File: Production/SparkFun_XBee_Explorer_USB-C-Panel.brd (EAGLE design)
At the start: 35.6 x 59.7 mm, 109 parts, among them J3 USB Female Type C Connector, J4 QWIIC_RIGHT_ANGLE, U2 AP63203, U5 ESD Diode, U7 FT231XS

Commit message: Adds Production Files
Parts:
- removed FRAME1: FRAME-LEDGER, SparkFun-Aesthetics:CREATIVE_COMMONS
- added ALED1, ALED2, ALED3, PLED1, PLED2, PLED3, RLED1, RLED2, RLED3, SHLD1, SHLD2, SHLD3: JUMPER-SMT_2_NC_TRACE_SILK, SparkFun-Jumpers:SMT-JUMPER_2_NC_TRACE_SILK
- added C13, C20, C22, C23, C27, C33, C35, C36, C40, C46, C48, C49: 0.1uF, SparkFun-Capacitors:0603
- added C15, C16, C28, C29, C41, C42: 22uF, SparkFun-Capacitors:0603
- added C17, C30, C43: 10uF, SparkFun-Capacitors:1210
- added C18, C19, C31, C32, C44, C45: 10nF, SparkFun-Capacitors:0603
- added C21, C34, C47: 10uF, SparkFun-Capacitors:0603
- added C24, C37, C50: 47pF, SparkFun-Capacitors:0603
- added C25, C38, C51: 10pF, SparkFun-Capacitors:0603
- added C26, C39, C52: 4.7uF, SparkFun-Capacitors:0603
- added D1, D10, D7: Red, SparkFun-LED:LED-0603
- added D11, D5, D8: BLUE, SparkFun-LED:LED-0603
- added D12, D6, D9: Yellow, SparkFun-LED:LED-0603
- added E$1, E$2, E$3, E$4: (no value), SparkFun-Aesthetics:FIDUCIAL-1X2
- added E$5, E$6: (no value), SparkFun-Retired:FIDUCIAL-1.5X3
- added FD10, FD11, FD12, FD13, FD14, FD15, FD16, FD5, FD6, FD7, FD8, FD9: FIDUCIAL1X2, SparkFun-Aesthetics:FIDUCIAL-1X2
- added H10, H11, H12, H13, H14, H15, H16, H5, H6, H7, H8, H9: STAND-OFFTIGHT, SparkFun-Hardware:STAND-OFF-TIGHT
- added I2C_PU1, I2C_PU2, I2C_PU3: JUMPER-SMT_3_2-NC_TRACE_SILK, SparkFun-Jumpers:SMT-JUMPER_3_2-NC_TRACE_SILK
- added J10, J16, J17, J23, J24, J9: (no value), SparkFun-Connectors:1X10_NO_SILK
- added J11, J18, J25: (no value), xbee_smart_modem:XBEE3-SMD
- added J12, J19, J26: USB Female Type C Connector, SparkFun-Connectors:USB-C-16P-4LAYER-ISOLATED
- added J13, J14, J20, J21, J27, J28: (no value), SparkFun-Connectors:1X01_NO_SILK_STAND
- added J15, J22, J7: QWIIC_RIGHT_ANGLE, SparkFun-Connectors:JST04_1MM_RA
- added L2, L3, L4: 3.9UH, SparkFun-Coils:INDUCTOR_3.9UH
- added LOGO10, LOGO7: OSHW-LOGOS, SparkFun-Aesthetics:OSHW-LOGO-S
- added LOGO11, LOGO5, LOGO8: QWIIC_LOGO_4MM, SparkFun-Aesthetics:QWIIC_4MM
- added LOGO12, LOGO6, LOGO9: SFE_LOGO_NAME.2_INCH, SparkFun-Aesthetics:SFE_LOGO_NAME_.2
- added R1, R10, R17, R18, R20, R22, R25, R26, R28, R30, R4, R6: 2.2k, SparkFun-Resistors:0603
- added R13, R16, R23, R24, R31, R32: 5.1k, SparkFun-Resistors:0603
- added R19, R27, R5: 4.7k, SparkFun-Resistors:0603
- added R21, R29, R9: 10k, SparkFun-Resistors:0603
- added S3, S4, S5, S6, S7, S8: (no value), SparkFun-Switches:TACTILE_SWITCH_SMD_5.2MM
- added U$100, U$125, U$154, U$179, U$208, U$71: (no value), topmirror:#GND#0
- added U$101, U$102, U$155, U$156, U$209, U$210: (no value), top:XBEE340
- added U$103, U$157, U$211: (no value), top:ASC32
- added U$104, U$158, U$212: (no value), top:RSSI31
- added U$105, U$159, U$213: (no value), top:PWR29
- added U$106, U$160, U$214: (no value), topmirror:#D1#AD1#SCL#8
- added U$107, U$108, U$161, U$162, U$215, U$216: (no value), top:EXPLORER1344
- added U$109, U$111, U$163, U$165, U$33, U$39: (no value), top:#3V3#1
- added U$110, U$164, U$34: (no value), top:#I2C#33
- added U$112, U$146, U$166, U$200, U$41, U$92: (no value), top:#VIN#4
- added U$113, U$167, U$42: (no value), bot:D03
- added U$114, U$168, U$43: (no value), top:#RST#30
- added U$115, U$169, U$47: (no value), SparkFun-Aesthetics:SFE_LOGO_NAME_.2
- added U$116, U$170, U$50: (no value), SparkFun-Aesthetics:SFE_LOGO_FLAME_.2
- added U$117, U$171, U$53: (no value), topmirror:#D0#AD0#18
- added U$118, U$172, U$55: (no value), topmirror:#D2#AD2#19
- added U$119, U$173, U$56: (no value), topmirror:#D3#AD3#23
- added U$120, U$174, U$57: (no value), topmirror:#D6##RTS##25
- added U$121, U$175, U$62: (no value), topmirror:#D5#ASSOC#25
- added U$122, U$176, U$68: (no value), topmirror:#D9##SLP##28
- added U$123, U$177, U$69: (no value), topmirror:#D7##CTS##26
- added U$124, U$178, U$70: (no value), topmirror:#D4#PICO#25
- added U$126, U$180, U$72: (no value), topmirror:#D8##DTR##27
- added U$127, U$181, U$73: (no value), topmirror:#RSSI#D10#17
- added U$128, U$182, U$74: (no value), topmirror:#SDA#D11#9
- added U$129, U$183, U$75: (no value), topmirror:##RST##15
- added U$130, U$184, U$76: (no value), topmirror:#POCI#D12#24
- added U$131, U$185, U$77: (no value), topmirror:#RXI#D14#15
- added U$132, U$186, U$78: (no value), topmirror:#TXO#D13#13
- added U$133, U$187, U$79: (no value), topmirror:#EN#17
- added U$134, U$188, U$80: (no value), topmirror:#ALED#21
- added U$135, U$189, U$81: (no value), topmirror:#RLED#22
- added U$136, U$190, U$82: (no value), topmirror:#PLED#20
- added U$137, U$191, U$83: (no value), botmirror:#TXO#8
- added U$138, U$192, U$84: (no value), botmirror:#RXI#7
- added U$139, U$193, U$85: (no value), botmirror:#POCI#32
- added U$140, U$194, U$86: (no value), botmirror:##RST##13
- added U$141, U$195, U$87: (no value), botmirror:##RTS##14
- added U$142, U$196, U$88: (no value), botmirror:##CS##26
- added U$143, U$197, U$89: (no value), botmirror:#SCLK#33
- added U$144, U$198, U$90: (no value), botmirror:#SCL#9
- added U$145, U$199, U$91: (no value), botmirror:#D0#3
- added U$147, U$201, U$93: (no value), botmirror:#EN#15
- added U$148, U$202, U$94: (no value), topmirror:#SHLD#36
- added U$149, U$203, U$95: (no value), topmirror:#NC#1
- added U$150, U$204, U$96: (no value), botmirror:#NC#3
- added U$151, U$152, U$205, U$206, U$97, U$98: (no value), topmirror:USB#C1342
- added U$153, U$207, U$99: (no value), topmirror:UART34
- added U1, U10, U6: AP63203, SparkFun-IC-Power:SOT23-6
- added U11, U3, U8: ESD Diode, SparkFun-DiscreteSemi:SOT-23-6
- added U12, U4, U9: FT231XS, SparkFun-IC-Comms:SSOP20_L
- LOGO4: value SPECIAL_INSTRUCTIONS-ORDERING -> OSHW-LOGOS; device SparkFun-Aesthetics:ORDERING_INSTRUCTIONS -> SparkFun-Aesthetics:OSHW-LOGO-S
- moved LOGO4 25.8 mm to (69.3, 53.0)
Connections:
- new net !RESET!1: C18.1, J10.5, J11.5, S3.1, S3.2
- new net !RESET!2: C31.1, J17.5, J18.5, S5.1, S5.2
- new net !RESET!3: C44.1, J24.5, J25.5, S7.1, S7.2
- new net 3.3V1: C15.1, C16.1, C19.1, C20.1, C21.1, C22.1, C23.1, C24.1, C25.1, C26.1, I2C_PU1.2, J10.1, J11.1, J7.2, L2.P$2, R5.1, U1.1, U4.13, U4.14, U4.15, U4.3
- new net 3.3V2: C28.1, C29.1, C32.1, C33.1, C34.1, C35.1, C36.1, C37.1, C38.1, C39.1, I2C_PU2.2, J15.2, J17.1, J18.1, L3.P$2, R19.1, U6.1, U9.13, U9.14, U9.15, U9.3
- new net 3.3V3: C41.1, C42.1, C45.1, C46.1, C47.1, C48.1, C49.1, C50.1, C51.1, C52.1, I2C_PU3.2, J22.2, J24.1, J25.1, L4.P$2, R27.1, U10.1, U12.13, U12.14, U12.15, U12.3
- new net D+1: J12.A6, J12.B6, U3.6, U4.11
- new net D+2: J19.A6, J19.B6, U8.6, U9.11
- new net D+3: J26.A6, J26.B6, U11.6, U12.11
- new net D-1: J12.A7, J12.B7, U3.4, U4.12
- new net D-2: J19.A7, J19.B7, U8.4, U9.12
- new net D-3: J26.A7, J26.B7, U11.4, U12.12
- new net D1: J11.20, J9.1, S4.1, S4.2
- new net D1/SCL1: J11.19, J7.4, J9.2, R4.1
- new net D1/SCL2: J15.4, J16.2, J18.19, R18.1
- new net D1/SCL3: J22.4, J23.2, J25.19, R26.1
- new net D10/RSSI_PWM1: J10.6, J11.6, R10.1
- new net D10/RSSI_PWM2: J17.6, J18.6, R22.1
- new net D10/RSSI_PWM3: J24.6, J25.6, R30.1
- new net D11/SDA1: J10.7, J11.7, J7.3, R1.1
- new net D11/SDA2: J15.3, J17.7, J18.7, R17.1
- new net D11/SDA3: J22.3, J24.7, J25.7, R25.1
- new net D12/SPI_POCI1: J10.4, J11.4
- new net D12/SPI_POCI2: J17.4, J18.4
- new net D12/SPI_POCI3: J24.4, J25.4
- new net D13/TXO1: J10.2, J11.2, U4.4
- new net D13/TXO2: J17.2, J18.2, U9.4
- new net D13/TXO3: J24.2, J25.2, U12.4
- new net D14/RXI1: J10.3, J11.3, U4.20
- new net D14/RXI2: J17.3, J18.3, U9.20
- new net D14/RXI3: J24.3, J25.3, U12.20
- new net D2: J16.1, J18.20, S6.1, S6.2
- new net D2/SPI_CLK1: J11.18, J9.3
- new net D2/SPI_CLK2: J16.3, J18.18
- new net D2/SPI_CLK3: J23.3, J25.18
- new net D3: J23.1, J25.20, S8.1, S8.2
- new net D3/SPI_!CS!1: J11.17, J9.4
- new net D3/SPI_!CS!2: J16.4, J18.17
- new net D3/SPI_!CS!3: J23.4, J25.17
- new net D4/SPI_PICO1: J11.11, J9.10
- new net D4/SPI_PICO2: J16.10, J18.11
- new net D4/SPI_PICO3: J23.10, J25.11
- new net D5/ASSOCIATE1: J11.15, J9.6, R6.1
- new net D5/ASSOCIATE2: J16.6, J18.15, R20.1
- new net D5/ASSOCIATE3: J23.6, J25.15, R28.1
- new net D6/!RTS!1: J11.16, J9.5, U4.2
- new net D6/!RTS!2: J16.5, J18.16, U9.2
- new net D6/!RTS!3: J23.5, J25.16, U12.2
- new net D7/!CTS!1: J11.12, J9.9, U4.9
- new net D7/!CTS!2: J16.9, J18.12, U9.9
- new net D7/!CTS!3: J23.9, J25.12, U12.9
- new net D8/!DTR!1: J10.9, J11.9, U4.1
- new net D8/!DTR!2: J17.9, J18.9, U9.1
- new net D8/!DTR!3: J24.9, J25.9, U12.1
- new net D9/!SLEEP!1: J11.13, J9.8
- new net D9/!SLEEP!2: J16.8, J18.13
- new net D9/!SLEEP!3: J23.8, J25.13
- new net EN1: J14.1, R9.1, U1.2
- new net EN2: J21.1, R21.1, U6.2
- new net EN3: J28.1, R29.1, U10.2
- new net GND1: ALED1.1, C15.2, C16.2, C17.2, C18.2, C19.2, C20.2, C21.2, C22.2, C23.2, C24.2, C25.2, C26.2, J10.10, J11.10, J12.GND, J12.GND2, J7.1, PLED1.1, R13.1, R16.1, RLED1.1, S3.3, S3.4, S4.3, S4.4, SHLD1.1, U1.4, U3.2, U4.16, U4.6
- new net GND2: ALED2.1, C28.2, C29.2, C30.2, C31.2, C32.2, C33.2, C34.2, C35.2, C36.2, C37.2, C38.2, C39.2, J15.1, J17.10, J18.10, J19.GND, J19.GND2, PLED2.1, R23.1, R24.1, RLED2.1, S5.3, S5.4, S6.3, S6.4, SHLD2.1, U6.4, U8.2, U9.16, U9.6
- new net GND3: ALED3.1, C41.2, C42.2, C43.2, C44.2, C45.2, C46.2, C47.2, C48.2, C49.2, C50.2, C51.2, C52.2, J22.1, J24.10, J25.10, J26.GND, J26.GND2, PLED3.1, R31.1, R32.1, RLED3.1, S7.3, S7.4, S8.3, S8.4, SHLD3.1, U10.4, U11.2, U12.16, U12.6
- new net N$10: D1.A, R5.2
- new net N$14: D5.A, R6.2
- new net N$15: ALED1.2, D5.C
- new net N$16: D1.C, PLED1.2
- new net N$17: C13.1, U1.6
- new net N$18: C13.2, L2.P$1, U1.5
- new net N$19: D6.A, R10.2
- new net N$20: D6.C, RLED1.2
- new net N$22: J12.B5, R16.2
- new net N$24: J12.A5, R13.2
- new net N$25: I2C_PU2.3, R17.2
- new net N$26: I2C_PU2.1, R18.2
- new net N$27: D7.A, R19.2
- new net N$28: D8.A, R20.2
- new net N$29: ALED2.2, D8.C
- new net N$30: D7.C, PLED2.2
- new net N$31: C27.1, U6.6
- new net N$32: C27.2, L3.P$1, U6.5
- new net N$33: D9.A, R22.2
- new net N$34: D9.C, RLED2.2
- new net N$35: J19.B5, R24.2
- new net N$36: J19.A5, R23.2
- new net N$37: I2C_PU3.3, R25.2
- new net N$38: I2C_PU3.1, R26.2
- new net N$39: D10.A, R27.2
- new net N$4: I2C_PU1.3, R1.2
- new net N$40: D11.A, R28.2
- new net N$41: ALED3.2, D11.C
- new net N$42: D10.C, PLED3.2
- new net N$43: C40.1, U10.6
- new net N$44: C40.2, L4.P$1, U10.5
- new net N$45: D12.A, R30.2
- new net N$46: D12.C, RLED3.2
- new net N$47: J26.B5, R32.2
- new net N$48: J26.A5, R31.2
- new net N$9: I2C_PU1.1, R4.2
- new net SHLD1: J12.SHLD1, J12.SHLD2, J12.SHLD3, J12.SHLD4, J12.SHLD5, J12.SHLD6, J12.SHLD7, J12.SHLD8, SHLD1.2
- new net SHLD2: J19.SHLD1, J19.SHLD2, J19.SHLD3, J19.SHLD4, J19.SHLD5, J19.SHLD6, J19.SHLD7, J19.SHLD8, SHLD2.2
- new net SHLD3: J26.SHLD1, J26.SHLD2, J26.SHLD3, J26.SHLD4, J26.SHLD5, J26.SHLD6, J26.SHLD7, J26.SHLD8, SHLD3.2
- new net VIN1: C17.1, J12.VBUS1, J12.VBUS2, J13.1, R9.2, U1.3, U3.5
- new net VIN2: C30.1, J19.VBUS1, J19.VBUS2, J20.1, R21.2, U6.3, U8.5
- new net VIN3: C43.1, J26.VBUS1, J26.VBUS2, J27.1, R29.2, U10.3, U11.5
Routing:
- net D14/RXI3: track 0.00 -> 47.7 mm, vias 0 -> 2
- net D14/RXI2: track 0.00 -> 47.7 mm, vias 0 -> 2
- net D14/RXI1: track 0.00 -> 47.7 mm, vias 0 -> 2
- net D1/SCL3: track 0.00 -> 45.4 mm
- net D1/SCL1: track 0.00 -> 45.4 mm
- net D1/SCL2: track 0.00 -> 45.4 mm
- net D11/SDA2: track 0.00 -> 45.1 mm, vias 0 -> 1
- net D11/SDA1: track 0.00 -> 45.1 mm, vias 0 -> 1
- net D11/SDA3: track 0.00 -> 45.1 mm, vias 0 -> 1
- net D10/RSSI_PWM2: track 0.00 -> 44.8 mm, vias 0 -> 3
- net D10/RSSI_PWM3: track 0.00 -> 44.8 mm, vias 0 -> 3
- net D10/RSSI_PWM1: track 0.00 -> 44.8 mm, vias 0 -> 3
- net D13/TXO3: track 0.00 -> 42.6 mm, vias 0 -> 2
- net D13/TXO2: track 0.00 -> 42.6 mm, vias 0 -> 2
- net D13/TXO1: track 0.00 -> 42.6 mm, vias 0 -> 2
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- added copper zone on layer 1, net 3.3V1
- added copper zone on layer 15, net 3.3V1
- added copper zone on layer 1, net 3.3V2
- added copper zone on layer 15, net 3.3V2
- added copper zone on layer 1, net 3.3V3
- added copper zone on layer 15, net 3.3V3
- added copper zone on layer 1, net GND1
- added copper zone on layer 16, net GND1
- added copper zone on layer 2, net GND1
- added copper zone on layer 1, net GND2
- added copper zone on layer 16, net GND2
- added copper zone on layer 2, net GND2
- added copper zone on layer 1, net GND3
- added copper zone on layer 16, net GND3
- added copper zone on layer 2, net GND3
- added copper zone on layer 1, net N$18
- added copper zone on layer 1, net N$32
- added copper zone on layer 1, net N$44
- added copper zone on layer 1, net SHLD1
- added copper zone on layer 15, net SHLD1
- added copper zone on layer 16, net SHLD1
- added copper zone on layer 2, net SHLD1
- added copper zone on layer 1, net SHLD2
- added copper zone on layer 15, net SHLD2
- added copper zone on layer 16, net SHLD2
- added copper zone on layer 2, net SHLD2
- added copper zone on layer 1, net SHLD3
- added copper zone on layer 15, net SHLD3
- added copper zone on layer 16, net SHLD3
- added copper zone on layer 2, net SHLD3
- added copper zone on layer 1, net VIN1
- added copper zone on layer 1, net VIN2
- added copper zone on layer 1, net VIN3
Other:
- board size 35.6 x 59.7 mm -> 157.5 x 87.9 mm
- board text added: "Route Out"
- board text added: "v-score"
- board text removed: "1.6mm Thickness"
- board text removed: "Elias Santistevan"
- board text removed: "Four Layer Board"
- board text removed: "Lead Free HASL"
- board text removed: "Units in Inches"

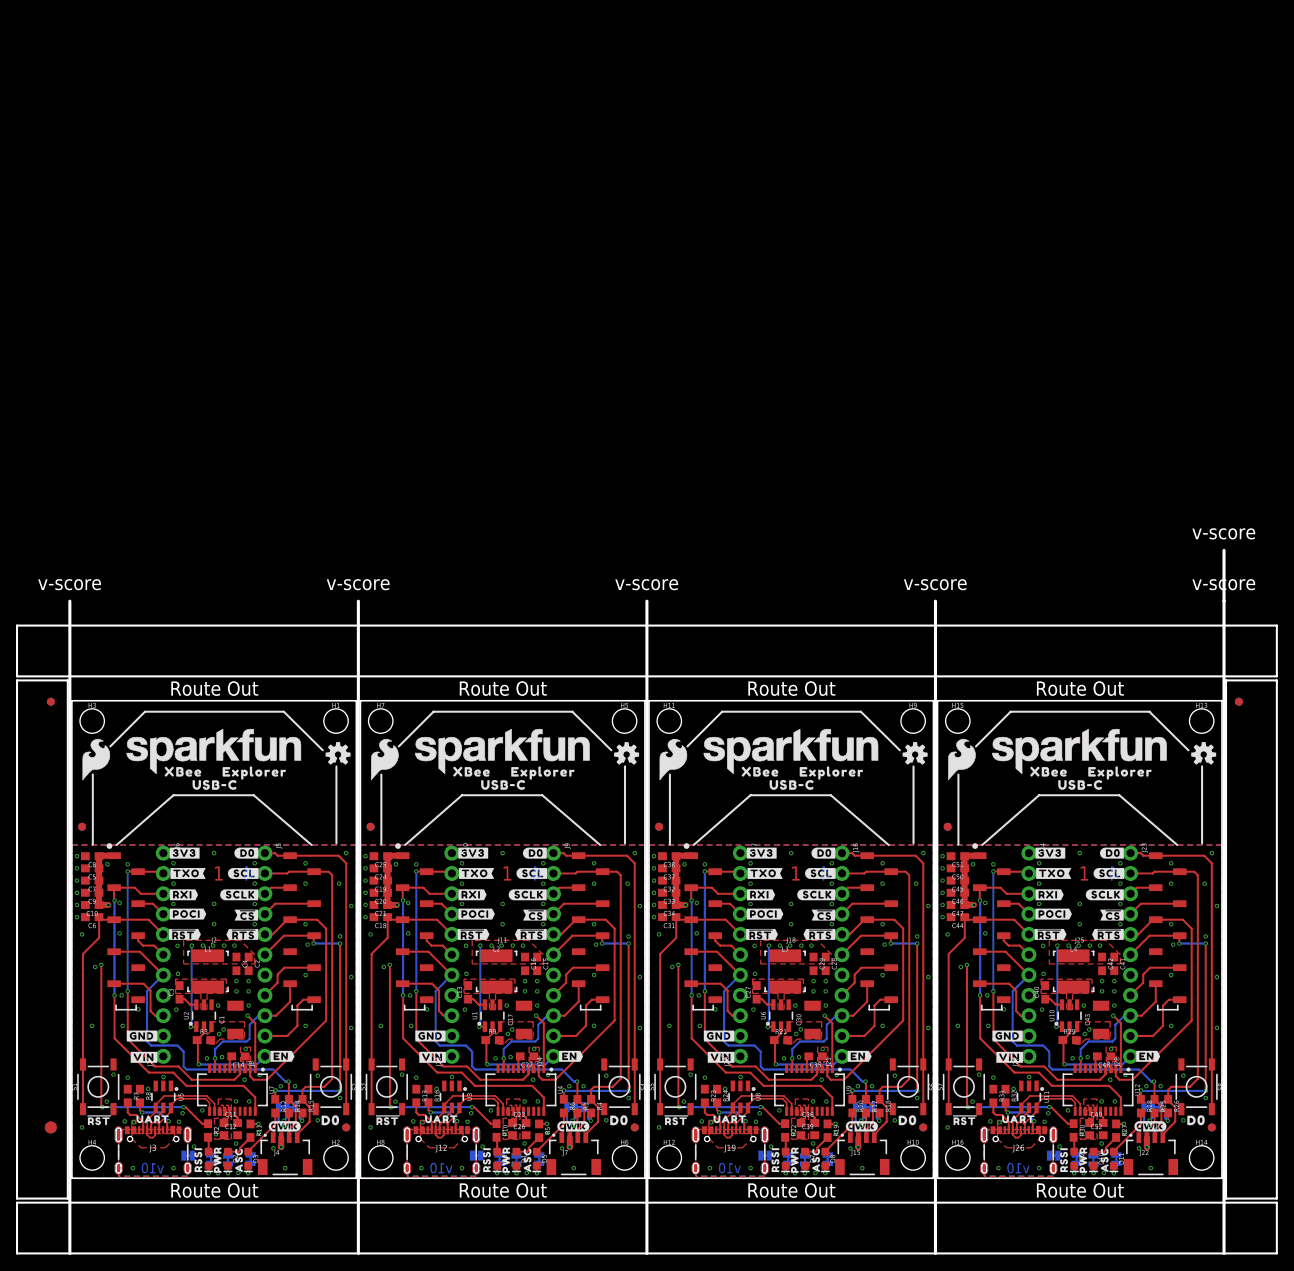
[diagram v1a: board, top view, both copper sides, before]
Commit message: Updates panel to be 3x2
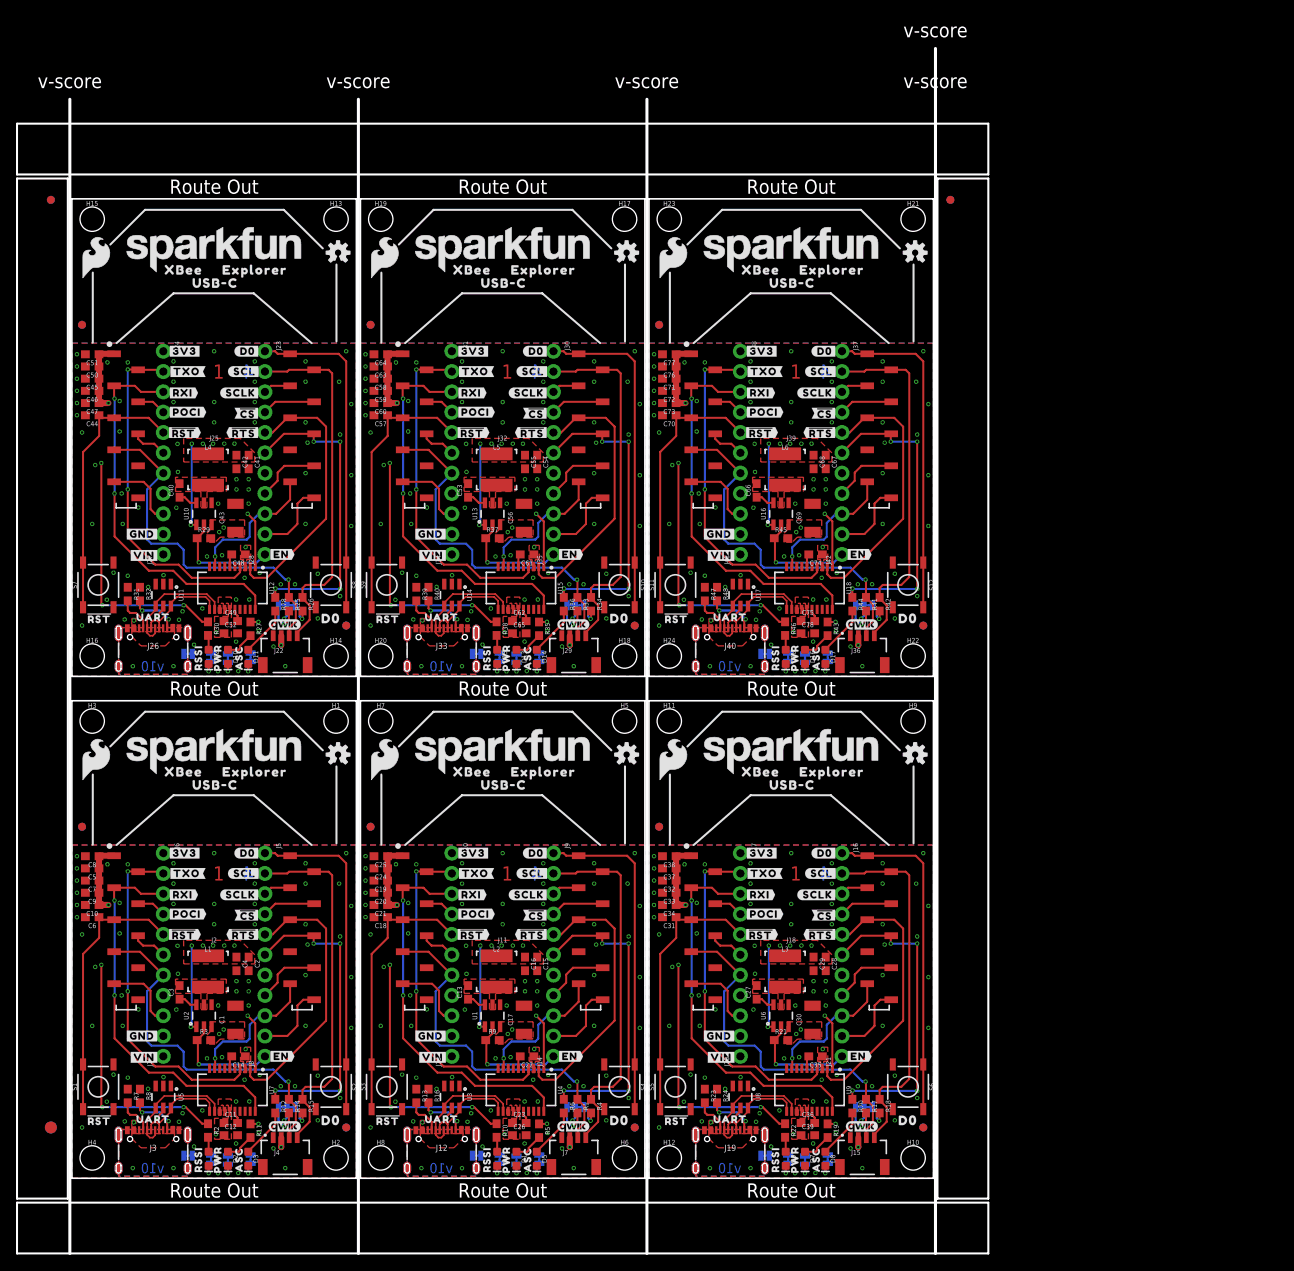
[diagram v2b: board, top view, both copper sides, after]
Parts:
- added ALED4, ALED5, PLED4, PLED5, RLED4, RLED5, SHLD4, SHLD5: JUMPER-SMT_2_NC_TRACE_SILK, SparkFun-Jumpers:SMT-JUMPER_2_NC_TRACE_SILK
- added C53, C59, C61, C62, C66, C72, C74, C75: 0.1uF, SparkFun-Capacitors:0603
- added C54, C55, C67, C68: 22uF, SparkFun-Capacitors:0603
- added C56, C69: 10uF, SparkFun-Capacitors:1210
- added C57, C58, C70, C71: 10nF, SparkFun-Capacitors:0603
- added C60, C73: 10uF, SparkFun-Capacitors:0603
- added C63, C76: 47pF, SparkFun-Capacitors:0603
- added C64, C77: 10pF, SparkFun-Capacitors:0603
- added C65, C78: 4.7uF, SparkFun-Capacitors:0603
- added D13, D16: Red, SparkFun-LED:LED-0603
- added D14, D17: BLUE, SparkFun-LED:LED-0603
- added D15, D18: Yellow, SparkFun-LED:LED-0603
- added FD17, FD18, FD19, FD20, FD21, FD22, FD23, FD24: FIDUCIAL1X2, SparkFun-Aesthetics:FIDUCIAL-1X2
- added H17, H18, H19, H20, H21, H22, H23, H24: STAND-OFFTIGHT, SparkFun-Hardware:STAND-OFF-TIGHT
- added I2C_PU4, I2C_PU5: JUMPER-SMT_3_2-NC_TRACE_SILK, SparkFun-Jumpers:SMT-JUMPER_3_2-NC_TRACE_SILK
- added J29, J36: QWIIC_RIGHT_ANGLE, SparkFun-Connectors:JST04_1MM_RA
- added J30, J31, J37, J38: (no value), SparkFun-Connectors:1X10_NO_SILK
- added J32, J39: (no value), xbee_smart_modem:XBEE3-SMD
- added J33, J40: USB Female Type C Connector, SparkFun-Connectors:USB-C-16P-4LAYER-ISOLATED
- added J34, J35, J41, J42: (no value), SparkFun-Connectors:1X01_NO_SILK_STAND
- added L5, L6: 3.9UH, SparkFun-Coils:INDUCTOR_3.9UH
- added LOGO13, LOGO16: OSHW-LOGOS, SparkFun-Aesthetics:OSHW-LOGO-S
- added LOGO14, LOGO17: QWIIC_LOGO_4MM, SparkFun-Aesthetics:QWIIC_4MM
- added LOGO15, LOGO18: SFE_LOGO_NAME.2_INCH, SparkFun-Aesthetics:SFE_LOGO_NAME_.2
- added R33, R34, R36, R38, R41, R42, R44, R46: 2.2k, SparkFun-Resistors:0603
- added R35, R43: 4.7k, SparkFun-Resistors:0603
- added R37, R45: 10k, SparkFun-Resistors:0603
- added R39, R40, R47, R48: 5.1k, SparkFun-Resistors:0603
- added S10, S11, S12, S9: (no value), SparkFun-Switches:TACTILE_SWITCH_SMD_5.2MM
- added U$217, U$219, U$271, U$273: (no value), top:#3V3#1
- added U$218, U$272: (no value), top:#I2C#33
- added U$220, U$254, U$274, U$308: (no value), top:#VIN#4
- added U$221, U$275: (no value), bot:D03
- added U$222, U$276: (no value), top:#RST#30
- added U$223, U$277: (no value), SparkFun-Aesthetics:SFE_LOGO_NAME_.2
- added U$224, U$278: (no value), SparkFun-Aesthetics:SFE_LOGO_FLAME_.2
- added U$225, U$279: (no value), topmirror:#D0#AD0#18
- added U$226, U$280: (no value), topmirror:#D2#AD2#19
- added U$227, U$281: (no value), topmirror:#D3#AD3#23
- added U$228, U$282: (no value), topmirror:#D6##RTS##25
- added U$229, U$283: (no value), topmirror:#D5#ASSOC#25
- added U$230, U$284: (no value), topmirror:#D9##SLP##28
- added U$231, U$285: (no value), topmirror:#D7##CTS##26
- added U$232, U$286: (no value), topmirror:#D4#PICO#25
- added U$233, U$262, U$287, U$316: (no value), topmirror:#GND#0
- added U$234, U$288: (no value), topmirror:#D8##DTR##27
- added U$235, U$289: (no value), topmirror:#RSSI#D10#17
- added U$236, U$290: (no value), topmirror:#SDA#D11#9
- added U$237, U$291: (no value), topmirror:##RST##15
- added U$238, U$292: (no value), topmirror:#POCI#D12#24
- added U$239, U$293: (no value), topmirror:#RXI#D14#15
- added U$240, U$294: (no value), topmirror:#TXO#D13#13
- added U$241, U$295: (no value), topmirror:#EN#17
- added U$242, U$296: (no value), topmirror:#ALED#21
- added U$243, U$297: (no value), topmirror:#RLED#22
- added U$244, U$298: (no value), topmirror:#PLED#20
- added U$245, U$299: (no value), botmirror:#TXO#8
- added U$246, U$300: (no value), botmirror:#RXI#7
- added U$247, U$301: (no value), botmirror:#POCI#32
- added U$248, U$302: (no value), botmirror:##RST##13
- added U$249, U$303: (no value), botmirror:##RTS##14
- added U$250, U$304: (no value), botmirror:##CS##26
- added U$251, U$305: (no value), botmirror:#SCLK#33
- added U$252, U$306: (no value), botmirror:#SCL#9
- added U$253, U$307: (no value), botmirror:#D0#3
- added U$255, U$309: (no value), botmirror:#EN#15
- added U$256, U$310: (no value), topmirror:#SHLD#36
- added U$257, U$311: (no value), topmirror:#NC#1
- added U$258, U$312: (no value), botmirror:#NC#3
- added U$259, U$260, U$313, U$314: (no value), topmirror:USB#C1342
- added U$261, U$315: (no value), topmirror:UART34
- added U$263, U$264, U$317, U$318: (no value), top:XBEE340
- added U$265, U$319: (no value), top:ASC32
- added U$266, U$320: (no value), top:RSSI31
- added U$267, U$321: (no value), top:PWR29
- added U$268, U$322: (no value), topmirror:#D1#AD1#SCL#8
- added U$269, U$270, U$323, U$324: (no value), top:EXPLORER1344
- added U13, U16: AP63203, SparkFun-IC-Power:SOT23-6
- added U14, U17: ESD Diode, SparkFun-DiscreteSemi:SOT-23-6
- added U15, U18: FT231XS, SparkFun-IC-Comms:SSOP20_L
- moved ALED3 125.1 mm to (22.4, 65.1)
- moved C43 125.1 mm to (20.4, 82.5)
- moved C48 125.1 mm to (20.8, 78.0)
- moved C49 125.1 mm to (19.9, 69.6)
- moved C52 125.1 mm to (19.9, 68.1)
- moved D10 125.1 mm to (19.5, 65.2)
- moved D11 125.1 mm to (22.0, 65.2)
- moved FD13 125.1 mm to (1.27, 106.7)
- moved FD14 125.1 mm to (1.27, 106.7)
- moved FD15 125.1 mm to (34.3, 69.1)
- moved FD16 125.1 mm to (34.3, 69.1)
- moved I2C_PU3 125.1 mm to (26.9, 71.6)
- moved J23 125.1 mm to (24.1, 103.4)
- moved J24 125.1 mm to (11.4, 103.4)
- moved J26 125.1 mm to (10.2, 69.1)
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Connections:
- new net !RESET!4: C57.1, J31.5, J32.5, S9.1, S9.2
- new net !RESET!5: C70.1, J38.5, J39.5, S11.1, S11.2
- new net 3.3V4: C54.1, C55.1, C58.1, C59.1, C60.1, C61.1, C62.1, C63.1, C64.1, C65.1, I2C_PU4.2, J29.2, J31.1, J32.1, L5.P$2, R35.1, U13.1, U15.13, U15.14, U15.15, U15.3
- new net 3.3V5: C67.1, C68.1, C71.1, C72.1, C73.1, C74.1, C75.1, C76.1, C77.1, C78.1, I2C_PU5.2, J36.2, J38.1, J39.1, L6.P$2, R43.1, U16.1, U18.13, U18.14, U18.15, U18.3
- new net D+4: J33.A6, J33.B6, U14.6, U15.11
- new net D+5: J40.A6, J40.B6, U17.6, U18.11
- new net D-4: J33.A7, J33.B7, U14.4, U15.12
- new net D-5: J40.A7, J40.B7, U17.4, U18.12
- new net D1/SCL4: J29.4, J30.2, J32.19, R34.1
- new net D1/SCL5: J36.4, J37.2, J39.19, R42.1
- new net D10/RSSI_PWM4: J31.6, J32.6, R38.1
- new net D10/RSSI_PWM5: J38.6, J39.6, R46.1
- new net D11/SDA4: J29.3, J31.7, J32.7, R33.1
- new net D11/SDA5: J36.3, J38.7, J39.7, R41.1
- new net D12/SPI_POCI4: J31.4, J32.4
- new net D12/SPI_POCI5: J38.4, J39.4
- new net D13/TXO4: J31.2, J32.2, U15.4
- new net D13/TXO5: J38.2, J39.2, U18.4
- new net D14/RXI4: J31.3, J32.3, U15.20
- new net D14/RXI5: J38.3, J39.3, U18.20
- new net D2/SPI_CLK4: J30.3, J32.18
- new net D2/SPI_CLK5: J37.3, J39.18
- new net D3/SPI_!CS!4: J30.4, J32.17
- new net D3/SPI_!CS!5: J37.4, J39.17
- new net D4: J30.1, J32.20, S10.1, S10.2
- new net D4/SPI_PICO4: J30.10, J32.11
- new net D4/SPI_PICO5: J37.10, J39.11
- new net D5: J37.1, J39.20, S12.1, S12.2
- new net D5/ASSOCIATE4: J30.6, J32.15, R36.1
- new net D5/ASSOCIATE5: J37.6, J39.15, R44.1
- new net D6/!RTS!4: J30.5, J32.16, U15.2
- new net D6/!RTS!5: J37.5, J39.16, U18.2
- new net D7/!CTS!4: J30.9, J32.12, U15.9
- new net D7/!CTS!5: J37.9, J39.12, U18.9
- new net D8/!DTR!4: J31.9, J32.9, U15.1
- new net D8/!DTR!5: J38.9, J39.9, U18.1
- new net D9/!SLEEP!4: J30.8, J32.13
- new net D9/!SLEEP!5: J37.8, J39.13
- new net EN4: J35.1, R37.1, U13.2
- new net EN5: J42.1, R45.1, U16.2
- new net GND4: ALED4.1, C54.2, C55.2, C56.2, C57.2, C58.2, C59.2, C60.2, C61.2, C62.2, C63.2, C64.2, C65.2, J29.1, J31.10, J32.10, J33.GND, J33.GND2, PLED4.1, R39.1, R40.1, RLED4.1, S10.3, S10.4, S9.3, S9.4, SHLD4.1, U13.4, U14.2, U15.16, U15.6
- new net GND5: ALED5.1, C67.2, C68.2, C69.2, C70.2, C71.2, C72.2, C73.2, C74.2, C75.2, C76.2, C77.2, C78.2, J36.1, J38.10, J39.10, J40.GND, J40.GND2, PLED5.1, R47.1, R48.1, RLED5.1, S11.3, S11.4, S12.3, S12.4, SHLD5.1, U16.4, U17.2, U18.16, U18.6
- new net N$49: I2C_PU4.3, R33.2
- new net N$50: I2C_PU4.1, R34.2
- new net N$51: D13.A, R35.2
- new net N$52: D14.A, R36.2
- new net N$53: ALED4.2, D14.C
- new net N$54: D13.C, PLED4.2
- new net N$55: C53.1, U13.6
- new net N$56: C53.2, L5.P$1, U13.5
- new net N$57: D15.A, R38.2
- new net N$58: D15.C, RLED4.2
- new net N$59: J33.B5, R40.2
- new net N$60: J33.A5, R39.2
- new net N$61: I2C_PU5.3, R41.2
- new net N$62: I2C_PU5.1, R42.2
- new net N$63: D16.A, R43.2
- new net N$64: D17.A, R44.2
- new net N$65: ALED5.2, D17.C
- new net N$66: D16.C, PLED5.2
- new net N$67: C66.1, U16.6
- new net N$68: C66.2, L6.P$1, U16.5
- new net N$69: D18.A, R46.2
- new net N$70: D18.C, RLED5.2
- new net N$71: J40.B5, R48.2
- new net N$72: J40.A5, R47.2
- new net SHLD4: J33.SHLD1, J33.SHLD2, J33.SHLD3, J33.SHLD4, J33.SHLD5, J33.SHLD6, J33.SHLD7, J33.SHLD8, SHLD4.2
- new net SHLD5: J40.SHLD1, J40.SHLD2, J40.SHLD3, J40.SHLD4, J40.SHLD5, J40.SHLD6, J40.SHLD7, J40.SHLD8, SHLD5.2
- new net VIN4: C56.1, J33.VBUS1, J33.VBUS2, J34.1, R37.2, U13.3, U14.5
- new net VIN5: C69.1, J40.VBUS1, J40.VBUS2, J41.1, R45.2, U16.3, U17.5
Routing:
- net D14/RXI5: track 0.00 -> 47.7 mm, vias 0 -> 2
- net D14/RXI4: track 0.00 -> 47.7 mm, vias 0 -> 2
- net D1/SCL4: track 0.00 -> 45.4 mm
- net D1/SCL5: track 0.00 -> 45.4 mm
- net D11/SDA5: track 0.00 -> 45.1 mm, vias 0 -> 1
- net D11/SDA4: track 0.00 -> 45.1 mm, vias 0 -> 1
- net D10/RSSI_PWM5: track 0.00 -> 44.8 mm, vias 0 -> 3
- net D10/RSSI_PWM4: track 0.00 -> 44.8 mm, vias 0 -> 3
- net D13/TXO5: track 0.00 -> 42.6 mm, vias 0 -> 2
- net D13/TXO4: track 0.00 -> 42.6 mm, vias 0 -> 2
- net D4: track 0.00 -> 41.4 mm
- net D5: track 0.00 -> 41.4 mm
- net D5/ASSOCIATE4: track 0.00 -> 39.1 mm, vias 0 -> 4
- net D5/ASSOCIATE5: track 0.00 -> 39.1 mm, vias 0 -> 4
- net D6/!RTS!4: track 0.00 -> 34.1 mm
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- added copper zone on layer 1, net 3.3V4
- added copper zone on layer 15, net 3.3V4
- added copper zone on layer 1, net 3.3V5
- added copper zone on layer 15, net 3.3V5
- added copper zone on layer 1, net GND4
- added copper zone on layer 16, net GND4
- added copper zone on layer 2, net GND4
- added copper zone on layer 1, net GND5
- added copper zone on layer 16, net GND5
- added copper zone on layer 2, net GND5
- added copper zone on layer 1, net N$56
- added copper zone on layer 1, net N$68
- added copper zone on layer 1, net SHLD4
- added copper zone on layer 15, net SHLD4
- added copper zone on layer 16, net SHLD4
- added copper zone on layer 2, net SHLD4
- added copper zone on layer 1, net SHLD5
- added copper zone on layer 15, net SHLD5
- added copper zone on layer 16, net SHLD5
- added copper zone on layer 2, net SHLD5
- added copper zone on layer 1, net VIN4
- added copper zone on layer 1, net VIN5
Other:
- board size 157.5 x 87.9 mm -> 121.4 x 150.6 mm
